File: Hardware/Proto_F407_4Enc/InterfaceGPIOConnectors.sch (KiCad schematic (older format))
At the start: 28 parts, among them J10 Conn_01x04, J11 Conn_01x04, J12 Conn_01x04, J13 Conn_01x04, J14 Conn_01x08, J15 Conn_01x08, J16 Conn_01x06, J17 Conn_01x04, J18 Conn_01x01, J19 Conn_ARM_JTAG_SWD_10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

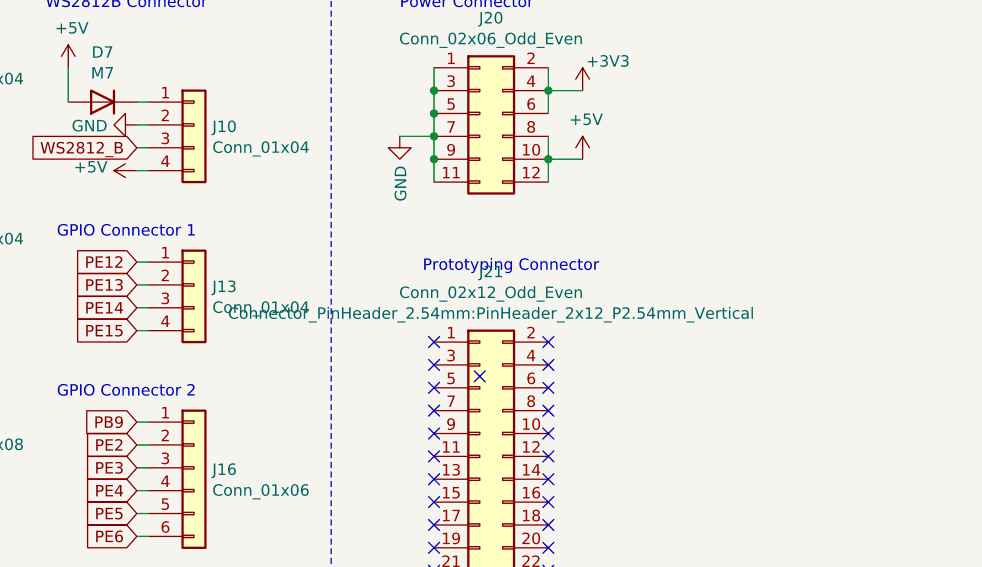
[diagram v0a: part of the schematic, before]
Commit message: minor label changes in schematic, added schematic + board image plots
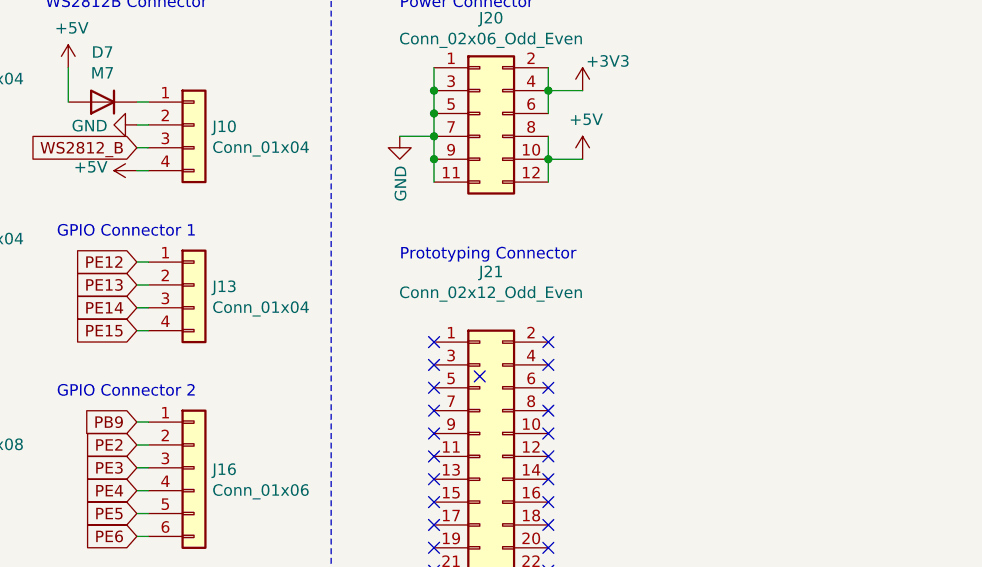
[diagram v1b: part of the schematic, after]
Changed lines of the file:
@@
 F 0 "J21" H 6050 6407 50  0000 C CNN
 F 1 "Conn_02x12_Odd_Even" H 6050 6316 50  0000 C CNN
-F 2 "Connector_PinHeader_2.54mm:PinHeader_2x12_P2.54mm_Vertical" H 6050 6225 50  0000 C CNN
+F 2 "Connector_PinHeader_2.54mm:PinHeader_2x12_P2.54mm_Vertical" V 6650 5650 50  0001 C CNN
 F 3 "~" H 6000 5600 50  0001 C CNN
 	1    6000 5600
 	1    0    0    -1
 $EndComp
-Text Notes 5750 4800 0    50   ~ 0
+Text Notes 5650 4750 0    50   ~ 0
 Prototyping Connector
 NoConn ~ 5800 5100
